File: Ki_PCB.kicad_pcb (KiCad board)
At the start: 2 copper layers, 65 x 65 mm, 70 parts, among them J1 0039301020, J2 B3B-XH-AM(LF)(SN), J3 0039301020, J4 0470531000, J5 4pin JST, J6 thermistor, Q1 SI2301-TP, Q2 SI2102A-TP, Q3 SI2102A-TP, Q4 SI2102A-TP, Q5 SI2102A-TP, Q6 SI2102A-TP, Q7 SI2102A-TP, Q8 SI2102A-TP, U1 LDL1117S50R, U2 TLC555CPWR, U3 MCP73844T-820I/MS, U4 BQ29209DRBR, U5 AP9101CK6, U6 AP9101CK6, U7 LM358, U8 TL5001CDR

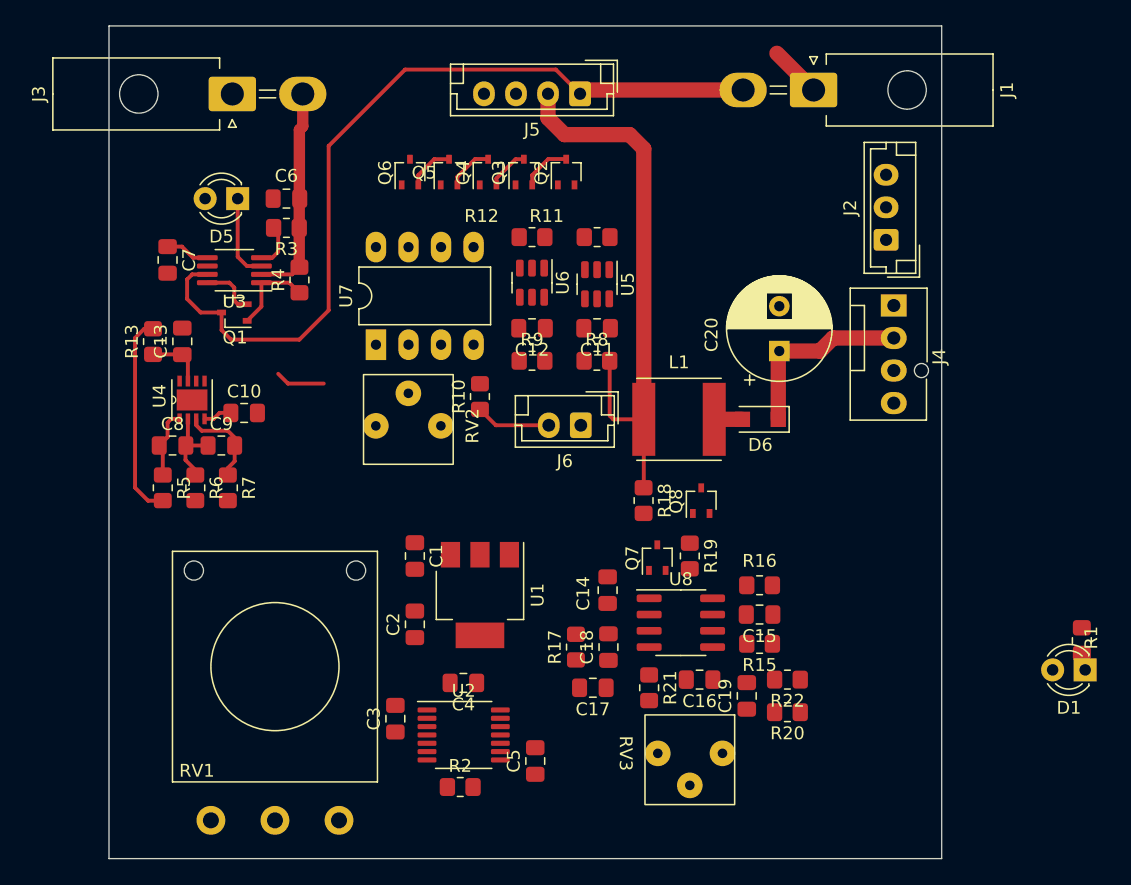
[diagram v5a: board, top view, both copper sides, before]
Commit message: layout 1 done, dsr errors with gnd plane clearances
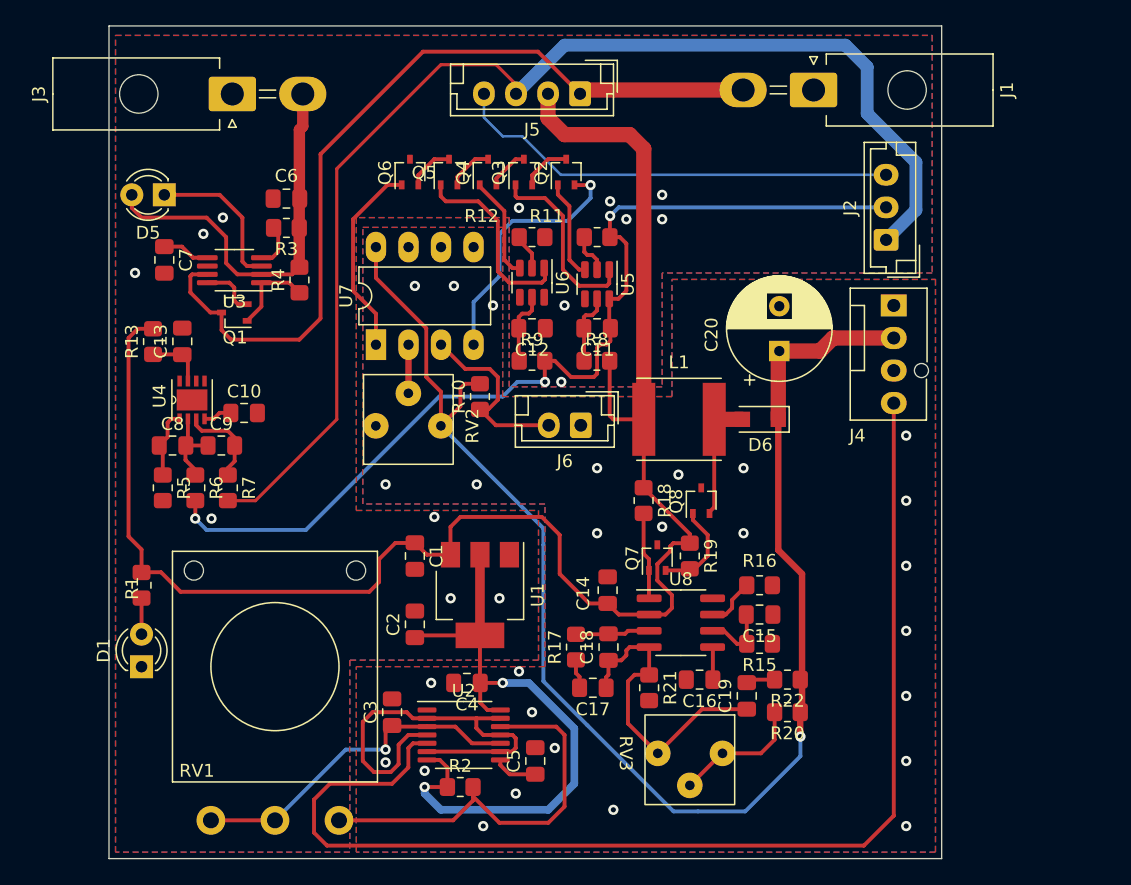
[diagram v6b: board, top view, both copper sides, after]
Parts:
- moved D1 73.7 mm to (75.0, 127.8), turned to 90 degrees
- moved R1 73.5 mm to (75.0, 121.5), turned to 90 degrees
- moved D5 5.73 mm to (76.8, 91.0)
- moved C3 0.57 mm to (94.6, 131.4)
- moved C4 0.28 mm to (100.4, 129.1)
- moved C7 0.25 mm to (76.8, 96.1)
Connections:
- J5 pad 4: /Batt_+ -> /Bal_batt +
- R5 pad 2: /SW_Batt + -> /Battery_protections/Bal_bat +
- R7 pad 2: GND -> /Bal_batt -
- U4 pad 6: /CHG + -> GND
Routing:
- net /12V: track 14.7 -> 112.4 mm, vias 0 -> 1
- net /Bal_batt -: track 0.00 -> 95.2 mm
- net /5V_PWM: track 0.00 -> 93.0 mm
- net /Bal_batt mid: track 0.00 -> 77.1 mm, vias 0 -> 3
- net /SW_Batt +: track 59.9 -> 130.7 mm
- net +5V: track 0.00 -> 50.4 mm, vias 0 -> 2
- net /Bal_batt +: track 0.00 -> 35.1 mm
- net Net-(U2-Pad11): track 0.00 -> 33.7 mm
- net Net-(R2-Pad2): track 0.00 -> 32.3 mm
- net Net-(C3-Pad1): track 0.00 -> 27.0 mm, vias 0 -> 1
- net /12V Boost converter/FB: track 0.00 -> 25.0 mm
- net /12V Boost converter/GND2: track 0.08 -> 20.1 mm, vias 0 -> 28
- net Net-(Q6-Pad1): track 0.00 -> 15.4 mm
- net /Battery_protections/DO_2: track 0.00 -> 15.1 mm
- net /Battery_protections/DO_1: track 0.00 -> 14.7 mm
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- added copper zone on B.Cu, net /12V Boost converter/GND2
- added copper zone on F.Cu, net /12V Boost converter/GND2
- added copper zone on B.Cu, net GND
- added copper zone on F.Cu, net GND

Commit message: 1st Gerber creatd  Please enter the commit message for your changes. Lines starting
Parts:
- added C8: 10uF, Capacitor_SMD:C_0805_2012Metric_Pad1.18x1.45mm_HandSolder, F.Cu at (77.8, 100.2)
- Q1: value SI2301-TP -> IRF7404; footprint Package_TO_SOT_SMD:SOT-323_SC-70 -> Package_SO:SOIC-8_3.9x4.9mm_P1.27mm
- moved Q1 4.34 mm to (84.4, 104.0), turned to -90 degrees
- moved R13 4.13 mm to (74.2, 106.3), turned to -90 degrees
- moved C14 2.42 mm to (76.5, 104.2)
- moved C11 1.77 mm to (83.1, 109.8)
- moved R6 1.77 mm to (79.3, 115.7)
- moved C10 1.77 mm to (81.3, 112.3)
- moved C9 1.77 mm to (77.5, 112.3)
- moved R5 1.77 mm to (76.8, 115.7)
- moved R7 1.77 mm to (81.9, 115.7)
- moved U4 1.77 mm to (79.1, 108.8)
- renumbered C9 to C10, C10 to C11, C11 to C12, C12 to C13, C13 to C14, C14 to C15, C15 to C16, C16 to C17, C17 to C18, C18 to C19, C19 to C20, C20 to C21, C8 to C9, D5 to D3, D6 to D4, R15 to R14, R16 to R15, R17 to R16, R18 to R17, R19 to R18, R20 to R19, R21 to R20, R22 to R21
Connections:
- net /Battery_protections/Bal_bat + renamed /Battery_protections/Bal_batt +
- D4 pad 2: Net-(D6-Pad2) -> Net-(D4-Pad2)
- L1 pad 2: Net-(D6-Pad2) -> Net-(D4-Pad2)
- Q1 pad 1: Net-(Q1-Pad1) -> Net-(R4-Pad1)
- Q1 pad 2: Net-(Q1-Pad2) -> Net-(R4-Pad1)
- Q1 pad 3: /Batt + -> Net-(R4-Pad1)
- Q3 pad 2: Net-(Q2-Pad3) -> Net-(Q3-Pad2)
- Q3 pad 3: Net-(Q3-Pad3) -> Net-(Q2-Pad3)
- Q4 pad 2: Net-(Q3-Pad3) -> Net-(Q3-Pad2)
- Q5 pad 2: Net-(Q4-Pad3) -> Net-(Q5-Pad2)
- Q5 pad 3: Net-(Q5-Pad3) -> Net-(Q4-Pad3)
- Q6 pad 2: Net-(Q5-Pad3) -> GND
- Q6 pad 3: GND -> Net-(Q5-Pad2)
- Q7 pad 2: Net-(Q7-Pad2) -> /12V Boost converter/GND2
- Q7 pad 3: /12V Boost converter/GND2 -> Net-(Q7-Pad3)
- Q8 pad 1: Net-(Q7-Pad2) -> Net-(Q7-Pad3)
- Q8 pad 2: Net-(D6-Pad2) -> /12V Boost converter/GND2
- Q8 pad 3: /12V Boost converter/GND2 -> Net-(D4-Pad2)
- R18 pad 2: Net-(Q7-Pad2) -> Net-(Q7-Pad3)
- R4 pad 1: Net-(Q1-Pad1) -> Net-(R4-Pad1)
- RV1 pad 1: Net-(C3-Pad1) -> Net-(R2-Pad2)
- RV1 pad 3: Net-(R2-Pad2) -> Net-(C3-Pad1)
- U3 pad 1: Net-(Q1-Pad1) -> Net-(R4-Pad1)
- U3 pad 8: Net-(Q1-Pad2) -> Net-(U3-Pad8)
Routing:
- net /5V_PWM: track 93.0 -> 80.1 mm
- net Net-(R2-Pad2): track 32.3 -> 43.8 mm, vias 0 -> 1
- net Net-(Q7-Pad3): track 0.00 -> 9.97 mm
- net Net-(D6-Pad2): track 9.70 -> 0.00 mm
- net Net-(R4-Pad1): track 0.00 -> 9.57 mm
- net Net-(D4-Pad2): track 0.00 -> 7.97 mm
- net /Batt +: track 66.4 -> 74.3 mm
- net Net-(Q7-Pad2): track 7.55 -> 0.00 mm
- net Net-(Q1-Pad1): track 6.73 -> 0.00 mm
- net Net-(U3-Pad8): track 0.00 -> 5.23 mm
- net Net-(Q5-Pad2): track 0.00 -> 4.81 mm
- net Net-(Q1-Pad2): track 4.40 -> 0.00 mm
- net /SW_Batt +: track 130.7 -> 126.7 mm
- net Net-(Q3-Pad2): track 0.00 -> 3.99 mm
- net Net-(Q5-Pad3): track 3.69 -> 0.00 mm
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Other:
- outline, holes or cut-outs redrawn
